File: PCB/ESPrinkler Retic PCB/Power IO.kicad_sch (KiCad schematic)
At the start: 32 parts, among them J6 Conn_01x04, Q1 AO3400A, Q2 AO3400A, U1 TPS5430DDA

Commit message: Modify SCH
Remote ~ from datasheet section and spelling mistake on parts list.

Swap status and wifi led control GPIOs for easier PCB traces
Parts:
- F1: Supplier LCSSC -> LCSC
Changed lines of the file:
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@@
 			)
 		)
-		(property "Supplier" "LCSSC"
+		(property "Supplier" "LCSC"
 			(at 44.45 49.53 0)
 			(effects
@@
 			)
 		)
-		(property "Datasheet" "~"
+		(property "Datasheet" ""
 			(at 20.32 92.71 0)
 			(effects

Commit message: Update Schematics
For all, update title block information.

Power IO:
- Change PTC fuse footprint reference
- Add part info for J1

Control Outputs:
- Add notes and box areas of schematic for clarity
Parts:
- F2: footprint Fuse:Fuse_BelFuse_0ZRE0100FF_L18.7mm_W5.1mm -> Fuse:Fuse_BelFuse_0ZRE0033FF_L11.4mm_W3.8mm
- J6: Manufacturer (none) -> DORABO; Manufacturer P/N (none) -> DB301V-5.0-4P-BU-S; Supplier (none) -> LCSC; Supplier P/N (none) -> C3034542
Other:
- title: (none) -> ESPrinkler Retic Controller
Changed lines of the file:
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@@
 	(generator_version "9.0")
 	(paper "A4")
+	(title_block
+		(title "ESPrinkler Retic Controller")
+		(date "2025-06-01")
+		(rev "1.0")
+	)
 	(text_box "Power Flags"
 		(exclude_from_sim no)
@@
 			)
 		)
-		(property "Manufacturer" ""
+		(property "Manufacturer" "DORABO"
 			(at 20.32 92.71 0)
 			(effects
@@
 			)
 		)
-		(property "Manufacturer P/N" ""
+		(property "Manufacturer P/N" "DB301V-5.0-4P-BU-S"
 			(at 20.32 92.71 0)
 			(effects
@@
 			)
 		)
-		(property "Supplier" ""
+		(property "Supplier" "LCSC"
 			(at 20.32 92.71 0)
 			(effects
@@
 			)
 		)
-		(property "Supplier P/N" ""
+		(property "Supplier P/N" "C3034542"
 			(at 20.32 92.71 0)
 			(effects
@@
 			)
 		)
-		(property "Footprint" "Fuse:Fuse_BelFuse_0ZRE0100FF_L18.7mm_W5.1mm"
+		(property "Footprint" "Fuse:Fuse_BelFuse_0ZRE0033FF_L11.4mm_W3.8mm"
 			(at 72.39 55.88 0)
 			(effects

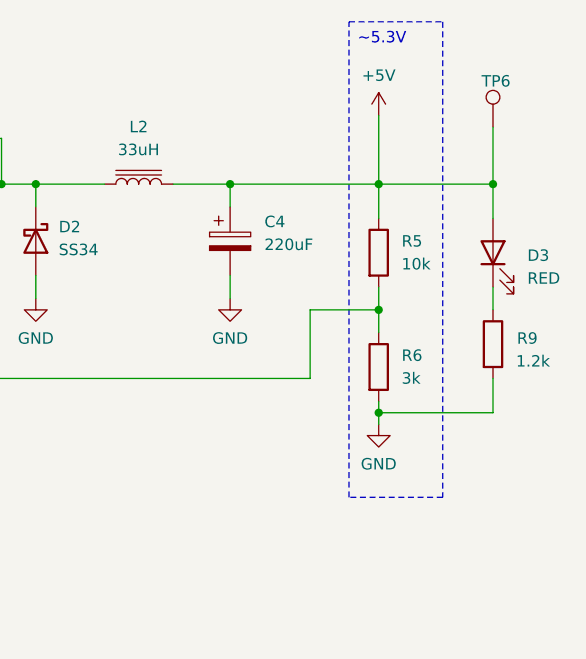
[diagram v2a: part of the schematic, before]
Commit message: Change FB array resistors
Change FB resistor values for step down converter, changing output voltage to be much closer to 5V.
Footprint of resistors changed.
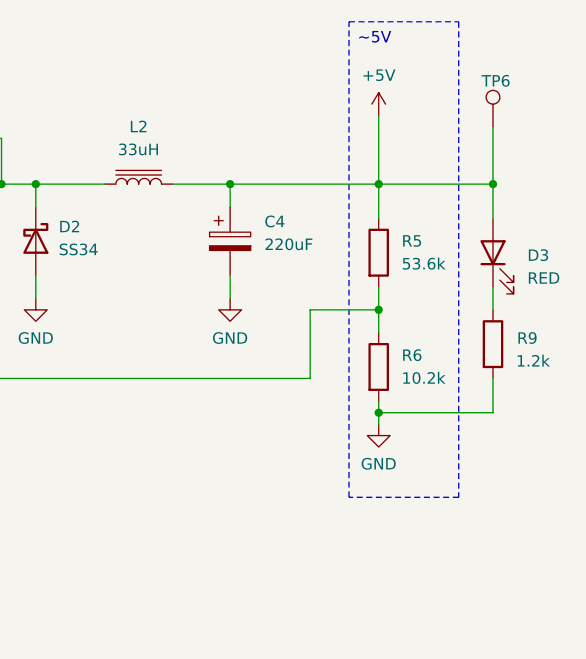
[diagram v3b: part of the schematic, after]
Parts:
- R5: value 10k -> 53.6k; footprint Resistor_SMD:R_0805_2012Metric -> Resistor_SMD:R_0603_1608Metric; Manufacturer P/N 0805W8F1002T5E -> 0603WAF5362T5E; Supplier P/N C17414 -> C23074
- R6: value 3k -> 10.2k; footprint Resistor_SMD:R_0805_2012Metric -> Resistor_SMD:R_0603_1608Metric; Manufacturer P/N 0805W8F3001T5E -> 0603WAF1022T5E; Supplier P/N C17661 -> C22772
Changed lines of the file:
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@@
 		)
 	)
-	(text_box "~5.3V"
+	(text_box "~5V"
 		(exclude_from_sim no)
 		(at 226.568 27.686 0)
-		(size 10.414 52.832)
+		(size 12.192 52.832)
 		(margins 0.9525 0.9525 0.9525 0.9525)
 		(stroke
@@
 			)
 		)
-		(property "Value" "10k"
+		(property "Value" "53.6k"
 			(at 232.41 54.6099 0)
 			(effects
@@
 			)
 		)
-		(property "Footprint" "Resistor_SMD:R_0805_2012Metric"
+		(property "Footprint" "Resistor_SMD:R_0603_1608Metric"
 			(at 228.092 53.34 90)
 			(effects
@@
 			)
 		)
-		(property "Manufacturer P/N" "0805W8F1002T5E"
+		(property "Manufacturer P/N" "0603WAF5362T5E"
 			(at 229.87 53.34 0)
 			(effects
@@
 			)
 		)
-		(property "Supplier P/N" "C17414"
+		(property "Supplier P/N" "C23074"
 			(at 229.87 53.34 0)
 			(effects
@@
 			)
 		)
-		(property "Value" "3k"
+		(property "Value" "10.2k"
 			(at 232.41 67.3099 0)
 			(effects
@@
 			)
 		)
-		(property "Footprint" "Resistor_SMD:R_0805_2012Metric"
+		(property "Footprint" "Resistor_SMD:R_0603_1608Metric"
 			(at 228.092 66.04 90)
 			(effects
@@
 			)
 		)
-		(property "Manufacturer P/N" "0805W8F3001T5E"
+		(property "Manufacturer P/N" "0603WAF1022T5E"
 			(at 229.87 66.04 0)
 			(effects
@@
 			)
 		)
-		(property "Supplier P/N" "C17661"
+		(property "Supplier P/N" "C22772"
 			(at 229.87 66.04 0)
 			(effects

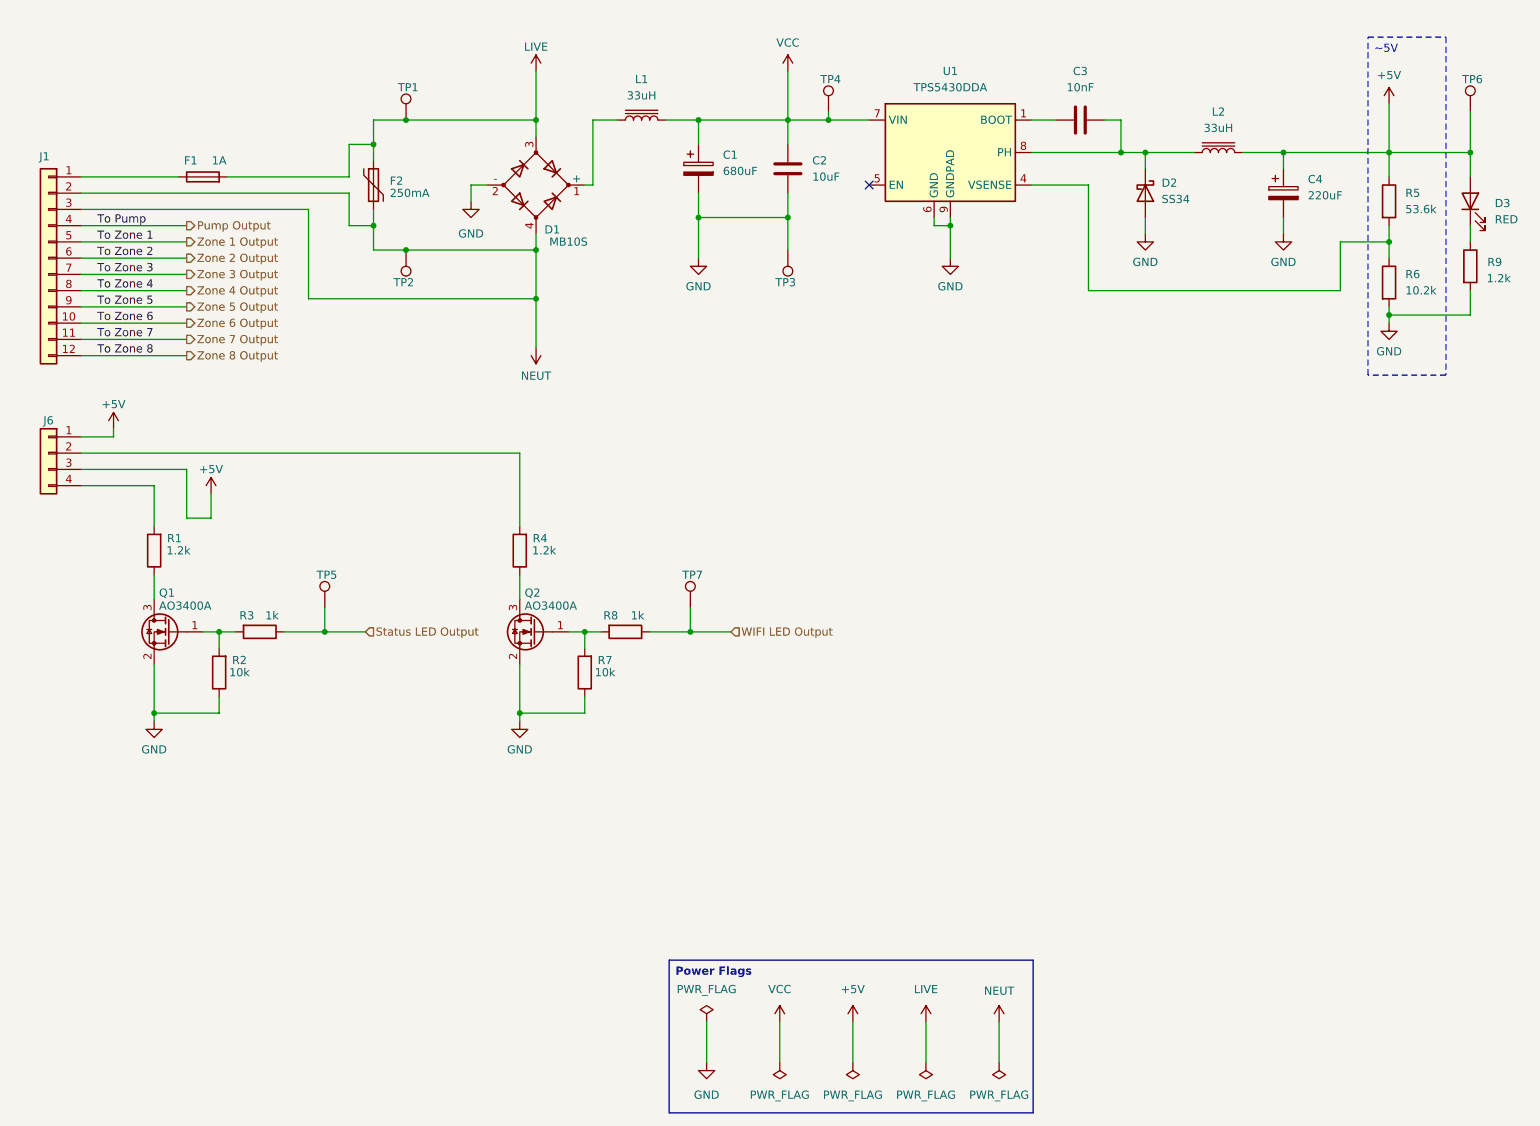
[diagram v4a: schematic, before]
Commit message: PCB version 1.1 following peer review
PTC in line with live, previously shorted between live and neutral.
Added boxes around sections on schematic for better readability.
Modified terminal block silkscreen to make more sense
Modified routing of 5V power to to reduce tunnels and traces on bottom plane.
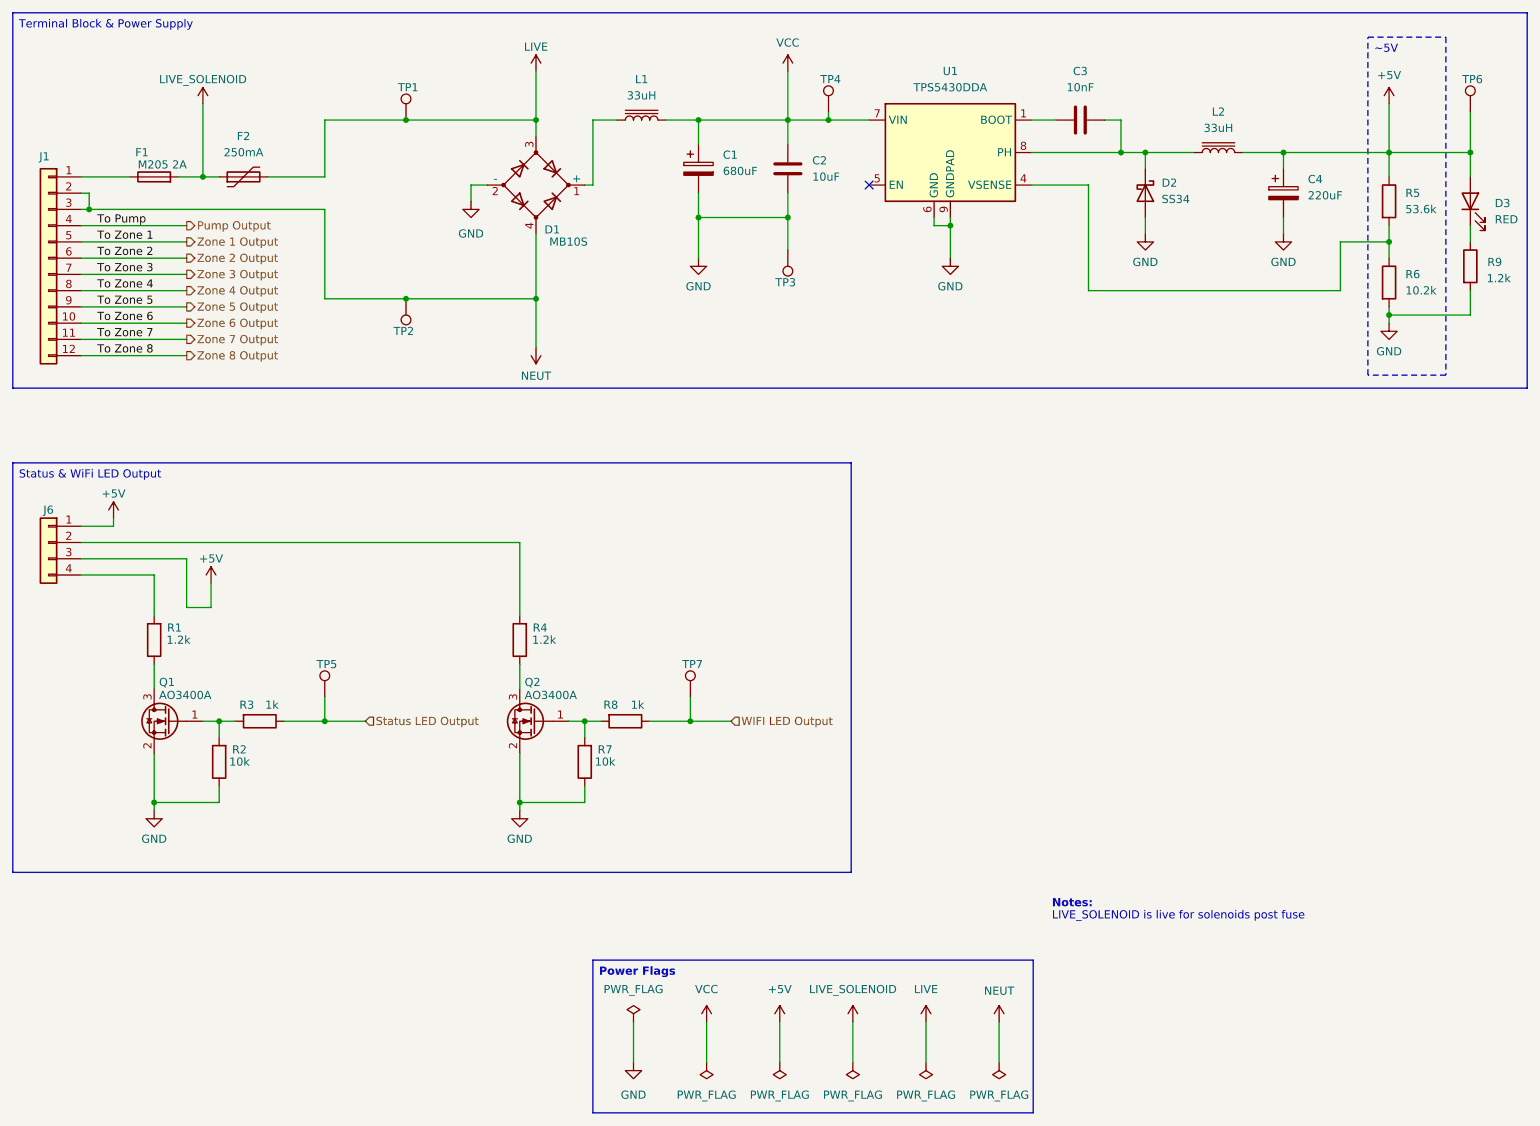
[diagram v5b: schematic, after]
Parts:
- F1: value 1A -> M205 2A
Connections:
- net LIVE: now also F2.2; no longer F1.2, F2.1
- net NEUT: no longer F2.2
- new net LIVE_SOLENOID: F1.2, F2.1
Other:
- note added: "LIVE_SOLENOID is live for solenoids post fuse"
- note added: "Notes:"
- moved on the sheet: F1, F2, J6, Q1, Q2, R1, R2, R3, R4, R7, R8, TP2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

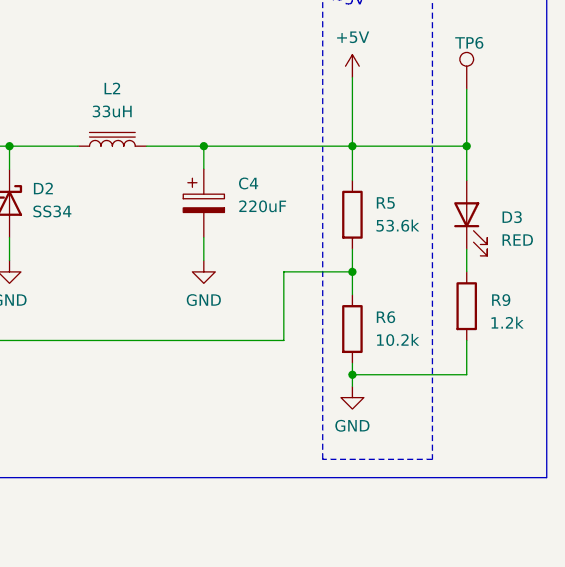
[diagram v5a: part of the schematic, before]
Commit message: Change SMPS voltage divider
Somehow managed to miscalculate the voltage divider resistor values to get 5V, getting 7V.

Change resistor values, change to 0805 footprint.
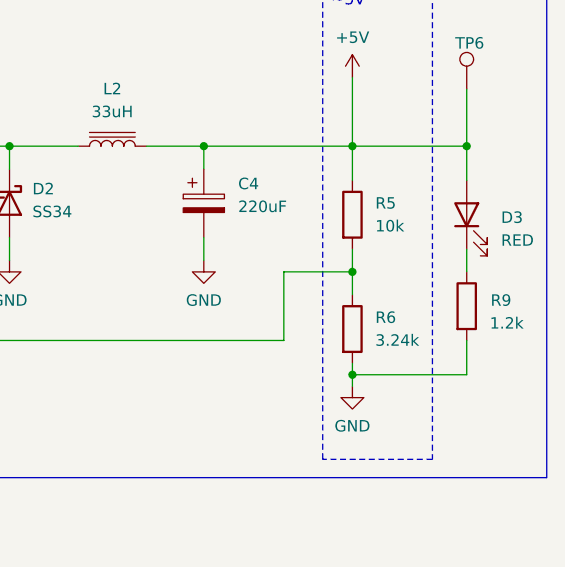
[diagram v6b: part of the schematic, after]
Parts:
- R5: value 53.6k -> 10k; footprint Resistor_SMD:R_0603_1608Metric -> Resistor_SMD:R_0805_2012Metric; Manufacturer P/N 0603WAF5362T5E -> 0805W8F1002T5E; Supplier P/N C23074 -> C17414
- R6: value 10.2k -> 3.24k; footprint Resistor_SMD:R_0603_1608Metric -> Resistor_SMD:R_0805_2012Metric; Manufacturer P/N 0603WAF1022T5E -> 0805W8F3241T5E; Supplier P/N C22772 -> C17609
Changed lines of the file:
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@@
 			)
 		)
-		(property "Value" "53.6k"
+		(property "Value" "10k"
 			(at 232.41 54.6099 0)
 			(effects
@@
 			)
 		)
-		(property "Footprint" "Resistor_SMD:R_0603_1608Metric"
+		(property "Footprint" "Resistor_SMD:R_0805_2012Metric"
 			(at 228.092 53.34 90)
 			(effects
@@
 			)
 		)
-		(property "Manufacturer P/N" "0603WAF5362T5E"
+		(property "Manufacturer P/N" "0805W8F1002T5E"
 			(at 229.87 53.34 0)
 			(effects
@@
 			)
 		)
-		(property "Supplier P/N" "C23074"
+		(property "Supplier P/N" "C17414"
 			(at 229.87 53.34 0)
 			(effects
@@
 			)
 		)
-		(property "Value" "10.2k"
+		(property "Value" "3.24k"
 			(at 232.41 67.3099 0)
 			(effects
@@
 			)
 		)
-		(property "Footprint" "Resistor_SMD:R_0603_1608Metric"
+		(property "Footprint" "Resistor_SMD:R_0805_2012Metric"
 			(at 228.092 66.04 90)
 			(effects
@@
 			)
 		)
-		(property "Description" "Resistor"
+		(property "Description" "125mW Thick Film Resistor 150V ±100ppm/℃ ±1% 3.24kΩ 0805 Chip Resistor - Surface Mount ROHS"
 			(at 229.87 66.04 0)
 			(effects
@@
 			)
 		)
-		(property "Manufacturer P/N" "0603WAF1022T5E"
+		(property "Manufacturer P/N" "0805W8F3241T5E"
 			(at 229.87 66.04 0)
 			(effects
@@
 			)
 		)
-		(property "Supplier P/N" "C22772"
+		(property "Supplier P/N" "C17609"
 			(at 229.87 66.04 0)
 			(effects

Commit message: Remove snubber and bring Kicad V10 update
Remove snubber from triac driver as its not required.

Attempt to start migrating to Kicad V10
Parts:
- J1: value ~ -> (none)
